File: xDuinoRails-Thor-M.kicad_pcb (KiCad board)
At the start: 6 copper layers, 30 x 20.1 mm, 46 parts, among them J701 Conn_02x11_Odd_Even, Q501 S8050, Q601 S8550, Q602 S8550, Q604 S8050, Q901 BSS138, Q902 BSS138, U1101 MOUDLE-SEEEDUINO-XIAO, U201 HT75xx-1-SOT89, U801 BDR6133

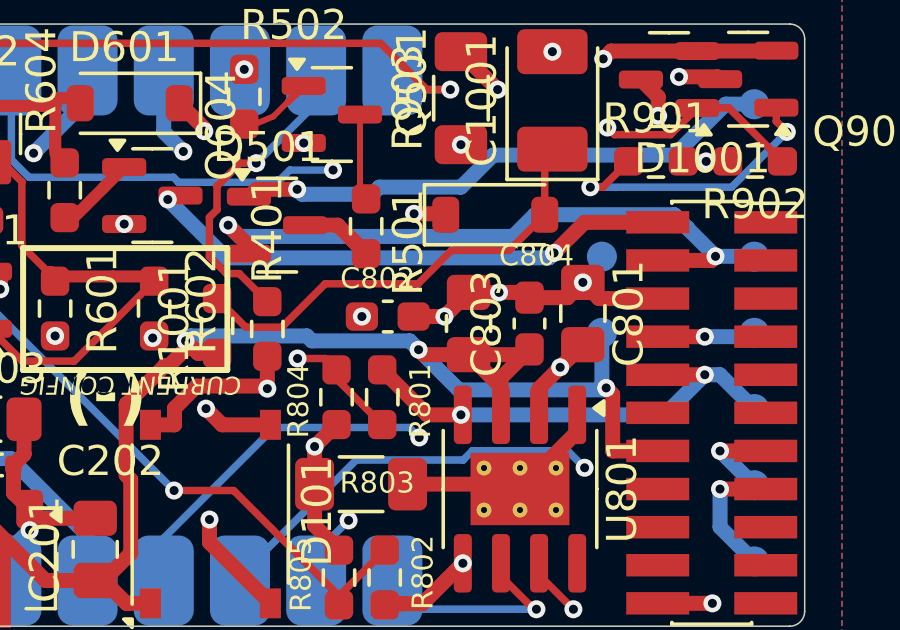
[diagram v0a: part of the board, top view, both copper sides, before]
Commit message: Fix - BOM errors
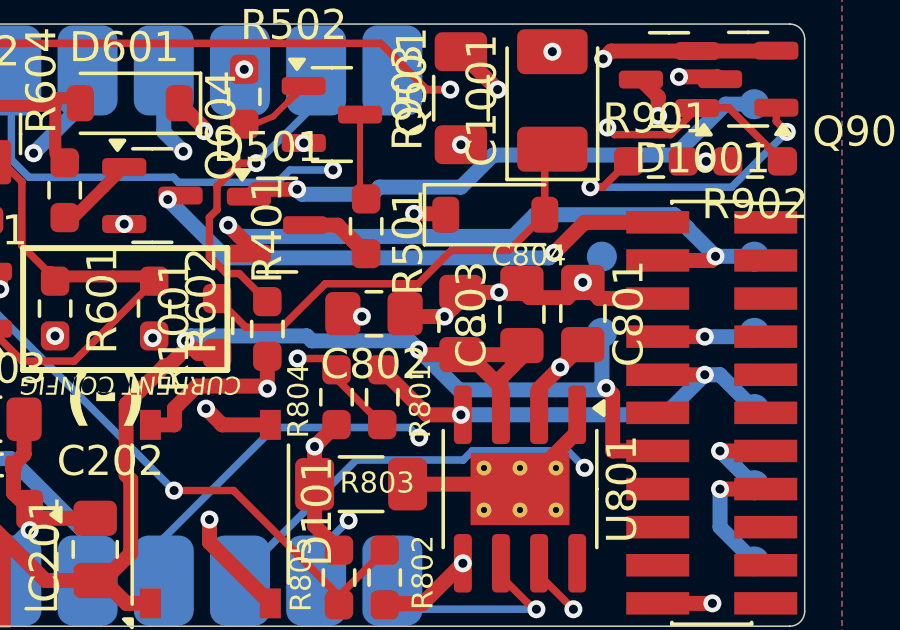
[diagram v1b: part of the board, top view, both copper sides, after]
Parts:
- C802, C803: footprint Capacitor_SMD:C_0603_1608Metric_Pad1.08x0.95mm_HandSolder -> Capacitor_SMD:C_0805_2012Metric_Pad1.18x1.45mm_HandSolder
- moved C802 0.47 mm to (158.6, 99.1)
- moved C803 0.40 mm to (163.6, 99.1)
- moved C804 0.25 mm to (161.5, 99.4)

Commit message: Fix - 3D model and some silkscreen
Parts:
- U801: footprint Package_SO:SOIC-8-1EP_3.9x4.9mm_P1.27mm_EP2.41x3.3mm_ThermalVias -> xDuinoRail:SOIC-8-1EP_3.9x4.9mm_P1.27mm_EP2.41x3.3mm_ThermalVias
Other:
- board text removed: "(-)"
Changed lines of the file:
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@@
 		)
 	)
-	(footprint "Package_SO:SOIC-8-1EP_3.9x4.9mm_P1.27mm_EP2.41x3.3mm_ThermalVias"
+	(footprint "xDuinoRail:SOIC-8-1EP_3.9x4.9mm_P1.27mm_EP2.41x3.3mm_ThermalVias"
 		(layer "F.Cu")
 		(at 163.513 104.902 -90)
@@
 		(tags "SOIC SO")
 		(property "Reference" "U801"
-			(at 0 -3.4 90)
+			(at 0 -3.4 -90)
 			(layer "F.SilkS")
 			(effects
@@
 		)
 		(property "Value" "BDR6133"
-			(at -0.416 0.191 90)
+			(at 0 3.4 -90)
 			(layer "F.Fab")
 			(effects
@@
 			)
 		)
-		(property "Footprint" "Package_SO:SOIC-8-1EP_3.9x4.9mm_P1.27mm_EP2.41x3.3mm_ThermalVias"
-			(at 0 0 90)
+		(property "Footprint" "xDuinoRail:SOIC-8-1EP_3.9x4.9mm_P1.27mm_EP2.41x3.3mm_ThermalVias"
+			(at 0 0 -90)
 			(layer "F.Fab")
 			(hide yes)
@@
 		)
 		(property "Datasheet" ""
-			(at 0 0 90)
+			(at 0 0 -90)
 			(layer "F.Fab")
 			(hide yes)
@@
 		)
 		(property "Description" ""
-			(at 0 0 90)
+			(at 0 0 -90)
 			(layer "F.Fab")
 			(hide yes)
@@
 		(attr smd)
 		(fp_line
-			(start 0 2.559999)
+			(start 0 2.56)
 			(end -1.95 2.56)
 			(stroke
@@
 		)
 		(fp_line
-			(start 0 2.559999)
+			(start 0 2.56)
 			(end 1.95 2.56)
 			(stroke
@@
 		)
 		(fp_line
-			(start 0 -2.559999)
+			(start 0 -2.56)
 			(end -1.95 -2.56)
 			(stroke
@@
 		)
 		(fp_line
-			(start 0 -2.559999)
+			(start 0 -2.56)
 			(end 1.95 -2.56)
 			(stroke
@@
 		(fp_poly
 			(pts
-				(xy -2.7 -2.465) (xy -2.939999 -2.795) (xy -2.46 -2.795) (xy -2.7 -2.465)
+				(xy -2.7 -2.465) (xy -2.94 -2.795) (xy -2.46 -2.795) (xy -2.7 -2.465)
 			)
 			(stroke
@@
 		(fp_line
 			(start -1.95 -1.475)
-			(end -0.975 -2.450001)
+			(end -0.975 -2.45)
 			(stroke
 				(width 0.1)
@@
 		)
 		(fp_line
-			(start 1.95 -2.45)
-			(end 1.95 2.45)
+			(start -0.975 -2.45)
+			(end 1.95 -2.45)
 			(stroke
 				(width 0.1)
@@
 		)
 		(fp_line
-			(start -0.975 -2.450001)
-			(end 1.95 -2.45)
+			(start 1.95 -2.45)
+			(end 1.95 2.45)
 			(stroke
 				(width 0.1)
@@
 		)
 		(fp_text user "${REFERENCE}"
-			(at 0 0 90)
+			(at 0 0 -90)
 			(layer "F.Fab")
 			(effects
@@
 			(drill 0.2)
 			(property pad_prop_heatsink)
-			(layers "*.Cu" "In5.Cu" "In6.Cu" "In7.Cu" "In8.Cu" "In9.Cu" "In10.Cu"
-				"In11.Cu" "In12.Cu" "In13.Cu" "In14.Cu" "In15.Cu" "In16.Cu" "In17.Cu"
-				"In18.Cu" "In19.Cu" "In20.Cu" "In21.Cu" "In22.Cu" "In23.Cu" "In24.Cu"
-				"In25.Cu" "In26.Cu" "In27.Cu" "In28.Cu" "In29.Cu" "In30.Cu"
-			)
+			(layers "*.Cu")
 			(remove_unused_layers no)
 			(net 39 "PGND")
@@
 			(drill 0.2)
 			(property pad_prop_heatsink)
-			(layers "*.Cu" "In5.Cu" "In6.Cu" "In7.Cu" "In8.Cu" "In9.Cu" "In10.Cu"
-				"In11.Cu" "In12.Cu" "In13.Cu" "In14.Cu" "In15.Cu" "In16.Cu" "In17.Cu"
-				"In18.Cu" "In19.Cu" "In20.Cu" "In21.Cu" "In22.Cu" "In23.Cu" "In24.Cu"
-				"In25.Cu" "In26.Cu" "In27.Cu" "In28.Cu" "In29.Cu" "In30.Cu"
-			)
+			(layers "*.Cu")
 			(remove_unused_layers no)
 			(net 39 "PGND")
@@
 			(drill 0.2)
 			(property pad_prop_heatsink)
-			(layers "*.Cu" "In5.Cu" "In6.Cu" "In7.Cu" "In8.Cu" "In9.Cu" "In10.Cu"
-				"In11.Cu" "In12.Cu" "In13.Cu" "In14.Cu" "In15.Cu" "In16.Cu" "In17.Cu"
-				"In18.Cu" "In19.Cu" "In20.Cu" "In21.Cu" "In22.Cu" "In23.Cu" "In24.Cu"
-				"In25.Cu" "In26.Cu" "In27.Cu" "In28.Cu" "In29.Cu" "In30.Cu"
-			)
+			(layers "*.Cu")
 			(remove_unused_layers no)
 			(net 39 "PGND")
@@
 			(drill 0.2)
 			(property pad_prop_heatsink)
-			(layers "*.Cu" "In5.Cu" "In6.Cu" "In7.Cu" "In8.Cu" "In9.Cu" "In10.Cu"
-				"In11.Cu" "In12.Cu" "In13.Cu" "In14.Cu" "In15.Cu" "In16.Cu" "In17.Cu"
-				"In18.Cu" "In19.Cu" "In20.Cu" "In21.Cu" "In22.Cu" "In23.Cu" "In24.Cu"
-				"In25.Cu" "In26.Cu" "In27.Cu" "In28.Cu" "In29.Cu" "In30.Cu"
-			)
+			(layers "*.Cu")
 			(remove_unused_layers no)
 			(net 39 "PGND")
@@
 			(drill 0.2)
 			(property pad_prop_heatsink)
-			(layers "*.Cu" "In5.Cu" "In6.Cu" "In7.Cu" "In8.Cu" "In9.Cu" "In10.Cu"
-				"In11.Cu" "In12.Cu" "In13.Cu" "In14.Cu" "In15.Cu" "In16.Cu" "In17.Cu"
-				"In18.Cu" "In19.Cu" "In20.Cu" "In21.Cu" "In22.Cu" "In23.Cu" "In24.Cu"
-				"In25.Cu" "In26.Cu" "In27.Cu" "In28.Cu" "In29.Cu" "In30.Cu"
-			)
+			(layers "*.Cu")
 			(remove_unused_layers no)
 			(net 39 "PGND")
@@
 			(drill 0.2)
 			(property pad_prop_heatsink)
-			(layers "*.Cu" "In5.Cu" "In6.Cu" "In7.Cu" "In8.Cu" "In9.Cu" "In10.Cu"
-				"In11.Cu" "In12.Cu" "In13.Cu" "In14.Cu" "In15.Cu" "In16.Cu" "In17.Cu"
-				"In18.Cu" "In19.Cu" "In20.Cu" "In21.Cu" "In22.Cu" "In23.Cu" "In24.Cu"
-				"In25.Cu" "In26.Cu" "In27.Cu" "In28.Cu" "In29.Cu" "In30.Cu"
-			)
+			(layers "*.Cu")
 			(remove_unused_layers no)
 			(net 39 "PGND")
@@
 			(pintype "power_in")
 		)
-		(model "${KICAD8_3DMODEL_DIR}/Package_SO.3dshapes/SOIC-8-1EP_3.9x4.9mm_P1.27mm_EP2.41x3.3mm.wrl"
+		(model "${KICAD8_3DMODEL_DIR}/Package_SO.3dshapes/SOIC-8-1EP_3.9x4.9mm_P1.27mm_EP2.29x3mm.wrl"
 			(offset
 				(xyz 0 0 0)
@@
 			)
 		)
-		(property "OLI_ID" "100nF_0603"
+		(property "OLI_ID" "100nF_0805"
 			(at 0 0 90)
 			(unlocked yes)
@@
 		(fp_arc
 			(start -6.600468 10.499999)
-			(mid -7.949608 10.111768)
+			(mid -7.949609 10.111769)
 			(end -8.812892 9.00468)
 			(stroke
@@
 		(fp_arc
 			(start 8.804034 9.001464)
-			(mid 7.944327 10.107119)
+			(mid 7.944325 10.107118)
 			(end 6.6 10.499999)
 			(stroke
@@
 			(layer "B.SilkS")
 		)
-		(fp_poly
-			(pts
-				(xy -11 12) (xy 11 12) (xy 11 -11) (xy -11 -11)
-			)
+		(fp_rect
+			(start -11 12)
+			(end 11 -11)
 			(stroke
 				(width 0.05)
@@
 		)
 		(pad "4" smd roundrect
-			(at -8.500001 0 270)
+			(at -8.5 0 270)
 			(size 3 2)
 			(layers "B.Cu" "B.Paste" "B.Mask")
@@
 		)
 		(pad "11" smd roundrect
-			(at 8.500001 0 270)
+			(at 8.5 0 270)
 			(size 3 2)
 			(layers "B.Cu" "B.Paste" "B.Mask")
@@
 			)
 		)
+		(model "${KIPRJMOD}/__lib/3d/SeeedStudio-XIAO_RP2040-v26.step"
+			(offset
+				(xyz 0 0 0)
+			)
+			(scale
+				(xyz 1 1 1)
+			)
+			(rotate
+				(xyz 0 0 0)
+			)
+		)
 	)
 	(footprint "TestPoint:TestPoint_Pad_D1.0mm"
@@
 		(layer "B.SilkS")
 	)
-	(gr_poly
-		(pts
-			(xy 153.756699 96.869666) (xy 153.756701 100.933665) (xy 146.9495 100.933665) (xy 146.9495 96.869665)
-		)
-		(stroke
-			(width 0.2)
-			(type default)
-		)
-		(fill none)
-		(layer "F.SilkS")
-	)
 	(gr_line
 		(start 143.502 89.402)
@@
 		)
 	)
-	(gr_text "(-)"
-		(at 148.336 101.0495 180)
-		(layer "F.SilkS")
-		(effects
-			(font
-				(size 1.5 1.5)
-				(thickness 0.3)
-				(bold yes)
-			)
-			(justify left bottom mirror)
-		)
-	)
 	(gr_text "Fehlender PIN"
 		(at 170.688 109.22 0)
@@
 		)
 	)
+	(group "subpcb_Stammblatt/rails_power_dc-dc-ldo-3v3_100mA"
+		(members "2495a32d-55d5-45c7-bf0d-90cec6114754" "8e28e822-f441-4a15-be24-b48dd8eb495f"
+			"f9515013-ffaf-46c4-ab7f-0578365a6d72"
+		)
+	)
 	(group "subpcb_Stammblatt/c9229de7/rails-signal-acknowledge_dcc"
 		(members "4c5602bf-903a-4ddb-8536-de0387f532e7" "507af063-49e9-4d2d-8016-8e7985a9710e"
@@
 		)
 	)
-	(group "subpcb_Stammblatt/rails_power_dc-dc-ldo-3v3_100mA"
-		(members "2495a32d-55d5-45c7-bf0d-90cec6114754" "8e28e822-f441-4a15-be24-b48dd8eb495f"
-			"f0e60a2e-b953-45e2-a762-24d2fcbf639e" "f9515013-ffaf-46c4-ab7f-0578365a6d72"
-		)
-	)
 	(group "subpcb_Stammblatt/c9229de7/rails_signal_feedback_dcc-railcom-8x50"
 		(members "16a319d4-62fd-400f-99ab-9c4439dc6ad6" "208636e3-d876-4511-90f1-8264a7ae489d"
 			"2632b471-c93b-4688-8365-79cd481cc3e8" "38a3be87-99bb-44d1-b52d-145a29fadfaa"
-			"4bb585cb-cc7d-4218-ab08-242a7052c194" "515018a4-f51e-4572-ba6b-e25c6693ea96"
-			"52c5a9b6-2cd8-4100-a4d3-4889c73e808a" "706dbf31-a91e-4c06-8680-1c9521f5667d"
-			"b876a4a8-a94f-404b-8d49-0ccdbbe68970" "e9b7c0d0-b788-44ec-a06f-fcc71b4ef725"
+			"515018a4-f51e-4572-ba6b-e25c6693ea96" "52c5a9b6-2cd8-4100-a4d3-4889c73e808a"
+			"706dbf31-a91e-4c06-8680-1c9521f5667d" "b876a4a8-a94f-404b-8d49-0ccdbbe68970"
+			"e9b7c0d0-b788-44ec-a06f-fcc71b4ef725"
 		)
 	)

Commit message: Chg - Draft of Plux16 connector
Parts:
- removed J701: Conn_02x11_Odd_Even, Connector_PinSocket_1.27mm:PinSocket_2x11_P1.27mm_Vertical_SMD
- removed TP401, TP402, TP403, TP404, TP405, TP406, TP407, TP701: ~, TestPoint:TestPoint_Pad_D1.0mm
- removed U1101: MOUDLE-SEEEDUINO-XIAO, xDuinoRail:XIAO_SMD
- added J1101: Conn_02x08_Odd_Even, Connector_PinHeader_1.27mm:PinHeader_2x08_P1.27mm_Vertical_SMD, F.Cu at (169.8, 100.7)
- added U1301: MOUDLE-SEEEDUINO-XIAO, xDuinoRail:XIAO_SMD, B.Cu at (151.6, 99.5)
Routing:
- net /AMP_FUNC1: track 19.2 -> 1.45 mm
- net /AMP_FUNC0: track 17.6 -> 1.49 mm
- net /AMP_MOTOR1: track 23.2 -> 11.0 mm
- net /DCC0: track 42.4 -> 32.5 mm, vias 4 -> 3
- net /AMP_MOTOR0: track 15.7 -> 7.88 mm
- net /+U: track 53.9 -> 48.3 mm, vias 4 -> 3
- net GND: track 27.2 -> 24.5 mm
- net /DCC1: vias 4 -> 5

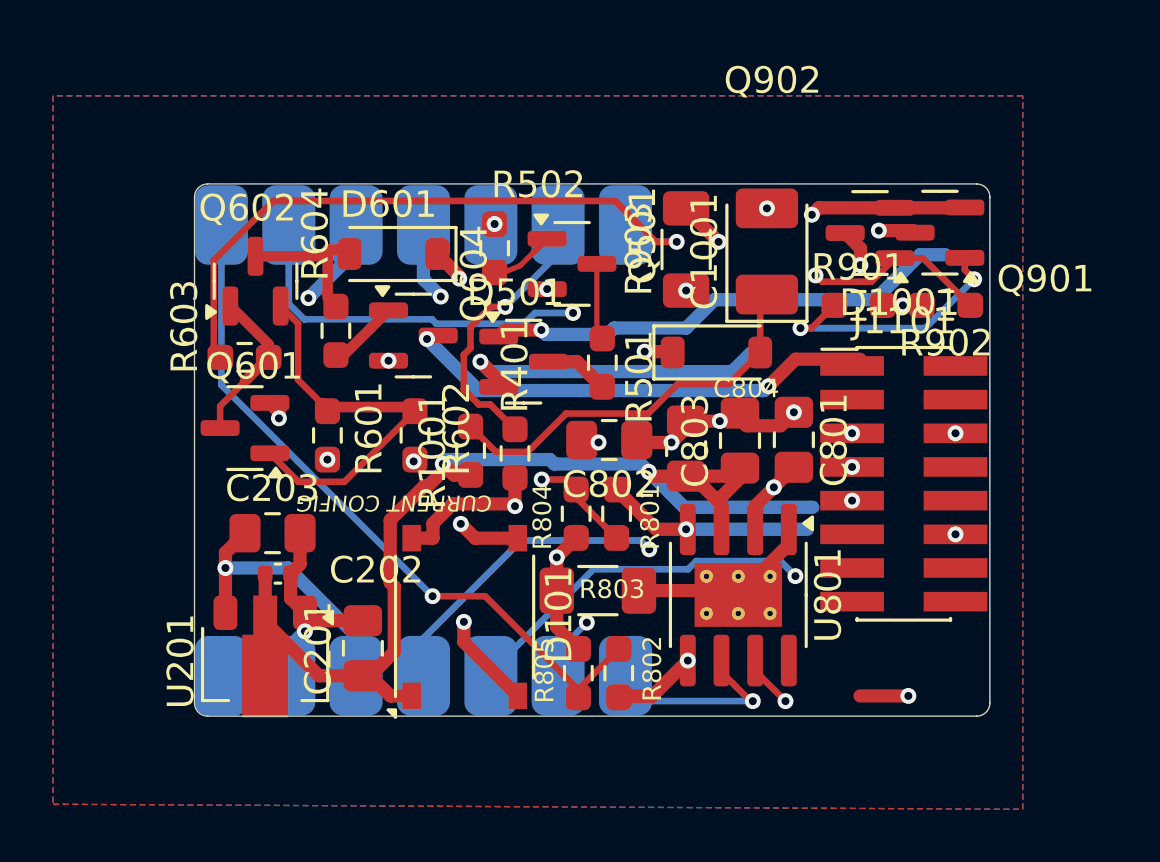
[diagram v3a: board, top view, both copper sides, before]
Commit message: Add - Routing of PluX16 connector
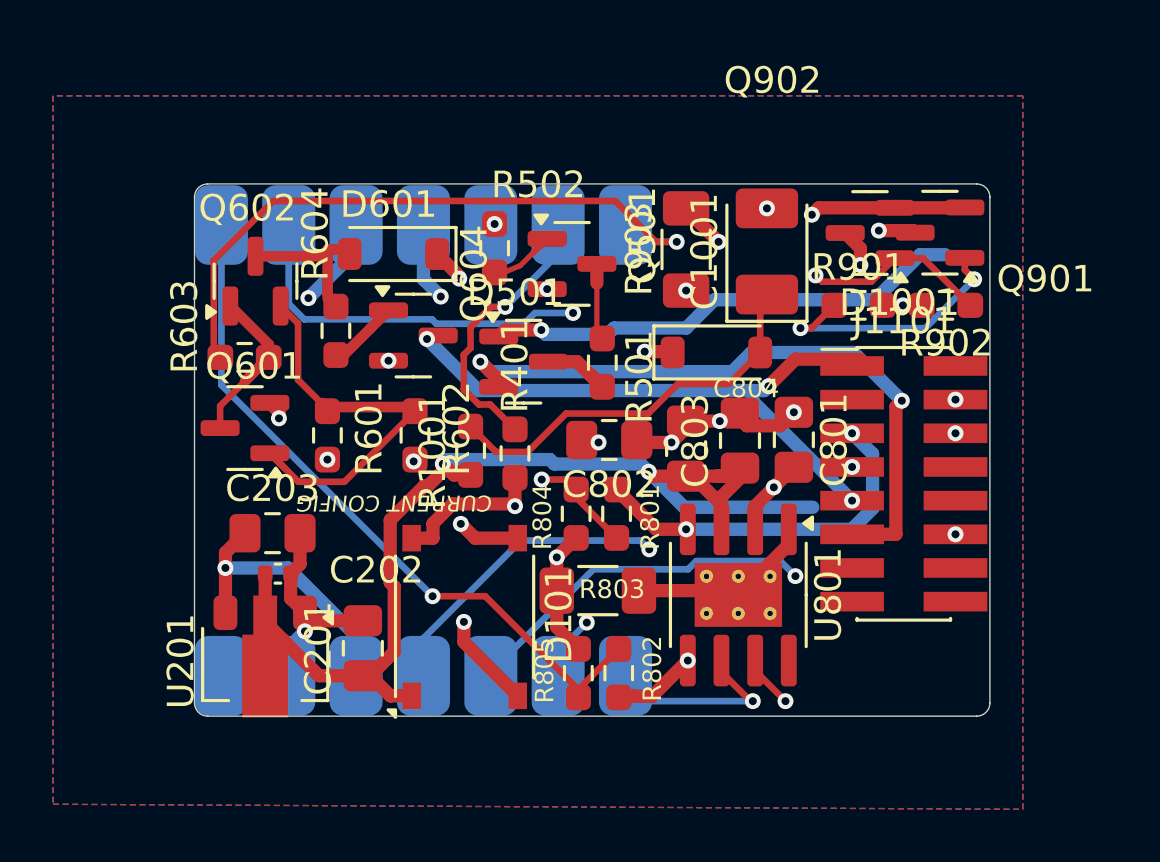
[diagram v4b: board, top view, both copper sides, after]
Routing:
- net /DCC0: track 32.5 -> 45.8 mm, vias 3 -> 4
- net /AMP_FUNC1: track 1.45 -> 13.1 mm
- net /AMP_FUNC0: track 1.49 -> 11.2 mm
- net /AMP_MOTOR1: track 11.0 -> 17.8 mm
- net /AMP_MOTOR0: track 7.88 -> 13.8 mm
- net /DCC1: track 53.3 -> 58.9 mm
- net /+3V3: track 16.5 -> 15.3 mm, vias 7 -> 6
- net /rails_signal_combined-medium/rails_signal_feedback_dcc-railcom-8x50/RC_CURR: track 16.7 -> 17.4 mm
- net /rails_signal_combined-medium/rails-signal-acknowledge_dcc/DCC+_DROP: track 2.88 -> 3.60 mm
- net /+U: track 48.3 -> 48.8 mm
- net GND: vias 11 -> 12

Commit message: Fix - ERC errors
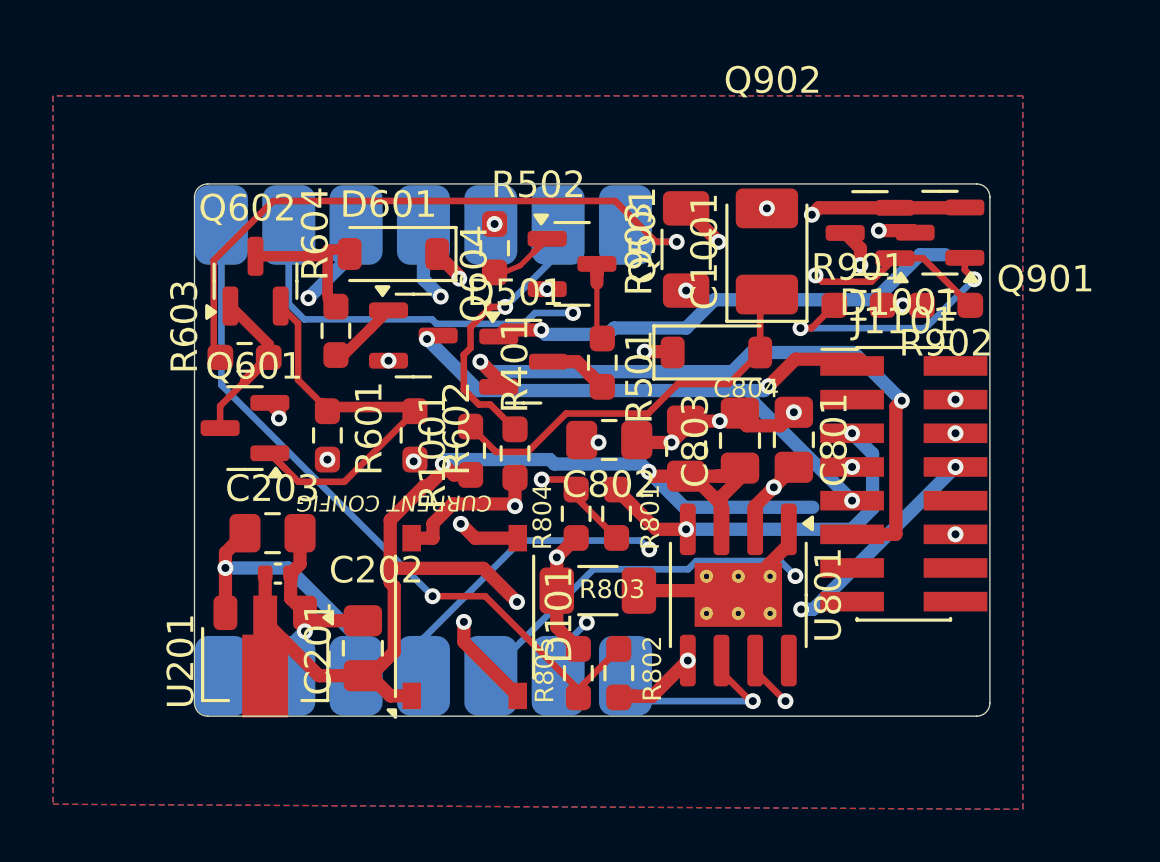
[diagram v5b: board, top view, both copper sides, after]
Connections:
- J1101 pad 8: /loco-adapters-2func/loco-adapter-nem658-plux16/U+ -> /+U
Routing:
- net /+U: track 48.8 -> 73.7 mm, vias 3 -> 6

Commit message: Add - Plux16 partnumber
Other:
- board text added: "xDRails Thor"
- board text removed: "Thor Medium"
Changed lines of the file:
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@@
 			)
 		)
+		(property "OLI_ID" "Plux16_02x08_1.27"
+			(at 0 0 0)
+			(unlocked yes)
+			(layer "F.Fab")
+			(hide yes)
+			(effects
+				(font
+					(size 1 1)
+					(thickness 0.15)
+				)
+			)
+		)
 		(property ki_fp_filters "Connector*:*_2x??_*")
 		(sheetname "loco-adapter-nem658-plux16")
@@
 		)
 	)
-	(gr_text "Thor Medium"
+	(gr_text "xDRails Thor"
 		(at 155.170857 104.521 0)
 		(layer "B.SilkS")
